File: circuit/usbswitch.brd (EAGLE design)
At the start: 100 x 80 mm, 11 parts, among them IC1 TINY25, Q2 BSA223SP

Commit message: cleanup
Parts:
- removed Q2: BSA223SP, irf:SO8
- added Q1: BSL207SP, irf:SOT23
- added R5, R6: 68, resistor:R1206
- moved D2 1.12 mm to (25.3, 34.6)
- moved R4 0.80 mm to (25.0, 31.9)
- moved D1 0.61 mm to (20.9, 33.9)
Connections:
- new net N$3: R5.2, X2.2
- new net N$8: R6.2, X2.3
- net N$1: now also Q1.1; no longer Q2.4
- net N$2: now also Q1.3; no longer Q2.5, Q2.6, Q2.7, Q2.8
- net VCC: now also Q1.2, R5.1, R6.1; no longer Q2.1, Q2.2, Q2.3
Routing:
- net VCC: track 27.9 -> 43.9 mm
- net N$2: track 18.5 -> 12.7 mm
- net N$3: track 0.00 -> 4.14 mm
- net N$8: track 0.00 -> 3.57 mm
- net N$1: track 2.72 -> 3.87 mm
- net N$4: track 22.9 -> 21.8 mm
- net N$5: track 9.86 -> 9.30 mm
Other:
- board size 100 x 80 mm -> 21.5 x 43.5 mm

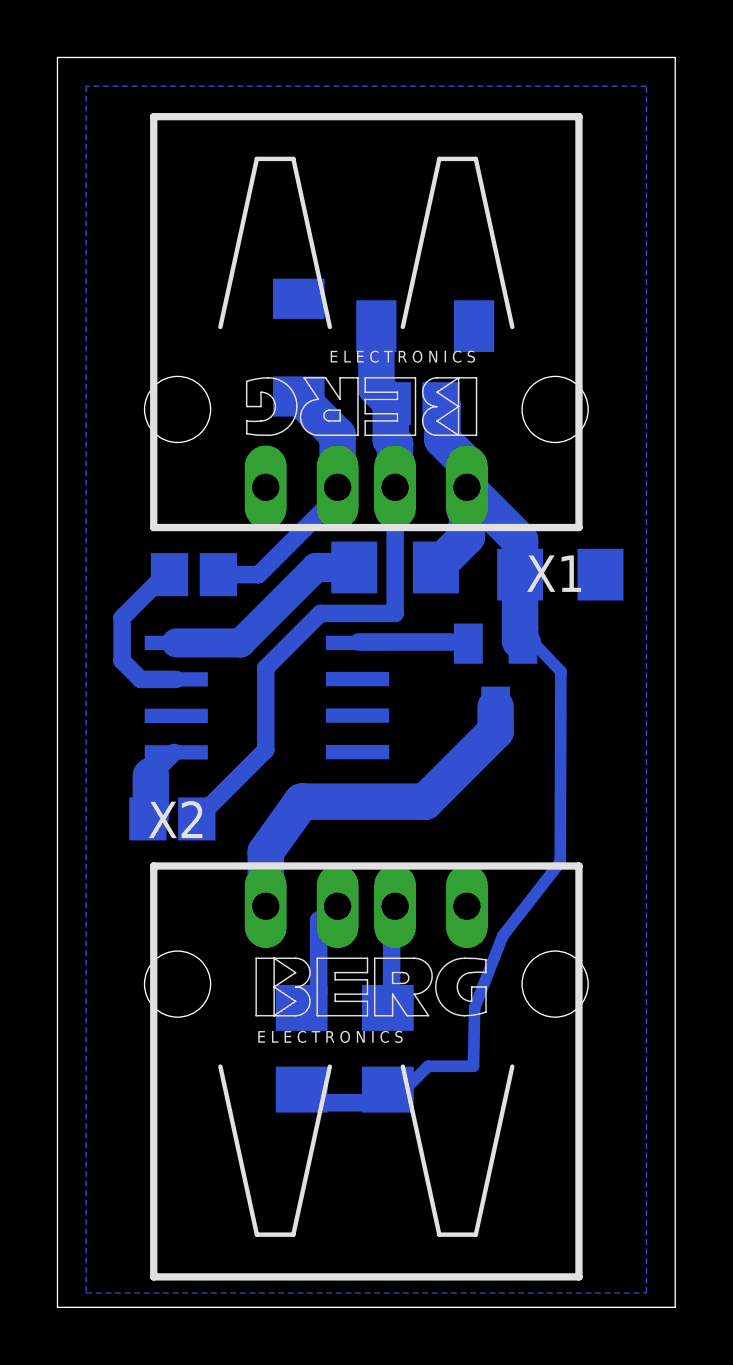
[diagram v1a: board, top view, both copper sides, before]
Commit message: Lessons learned from first smd prototype
* turned USB connector to PC around
* made all resistors 1206 types
* still need to fix transistor stuff...
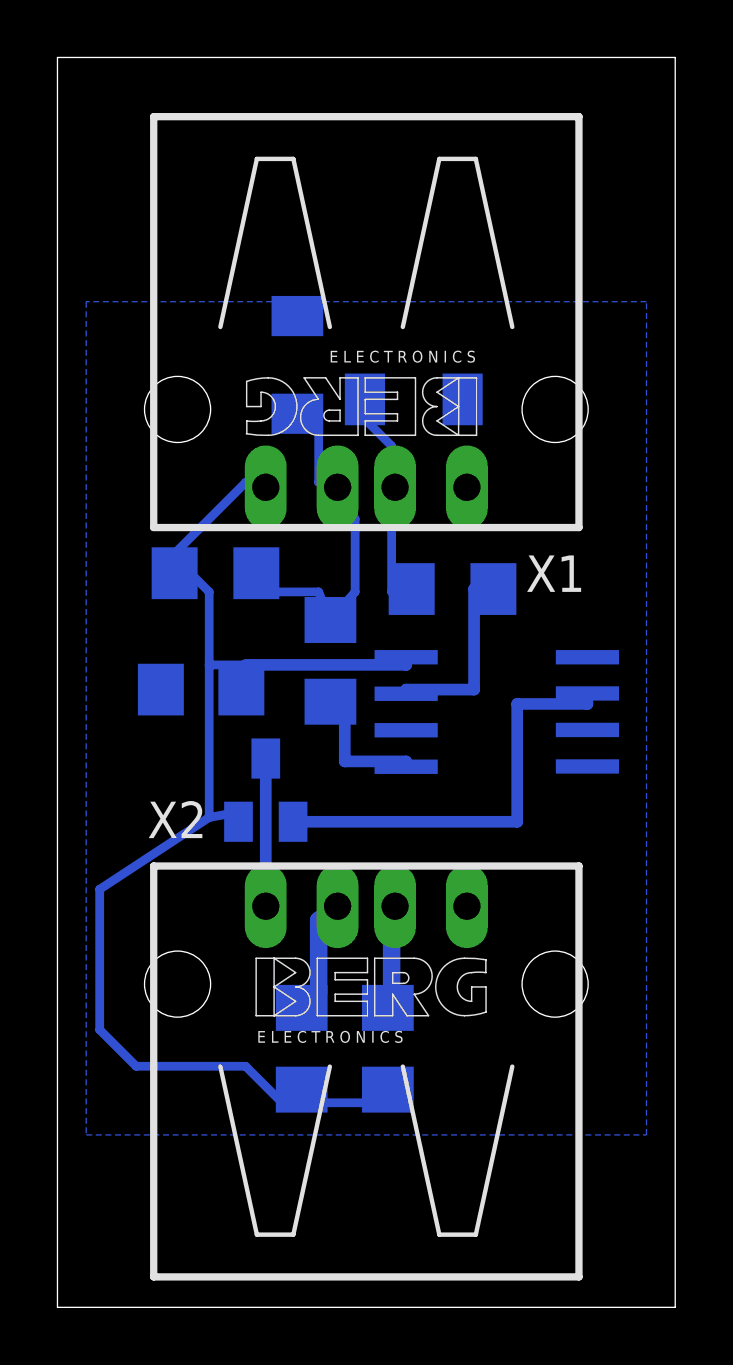
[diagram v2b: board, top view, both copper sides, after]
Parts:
- removed R1: 68, resistor:R1206
- R2, R3, R4: device resistor:R0805 -> rcl:R1206
- R6: device resistor:R1206 -> rcl:R1206
- moved C1 13.1 mm to (17.5, 22.0), turned to 0 degrees
- moved R4 9.15 mm to (18.0, 26.1), turned to 0 degrees
- moved R3 9.01 mm to (26.2, 25.5), turned to 180 degrees
- moved Q1 8.94 mm to (19.8, 18.5), turned to 0 degrees
- moved IC1 8.02 mm to (27.8, 21.2)
- moved R2 7.78 mm to (22.0, 23.0), turned to 270 degrees
- moved D2 4.65 mm to (20.9, 33.3), turned to 90 degrees
- moved D1 4.39 mm to (24.9, 32.1), turned to 180 degrees
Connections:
- net GND: now also X1.1; no longer X1.4
- net N$1: now also IC1.2; no longer IC1.1
- net N$4: now also X1.3; no longer X1.2
- net N$5: now also X1.2; no longer X1.3
- net VCC: now also X1.4; no longer R1.1, R1.2, X1.1
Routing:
- net N$1: track 3.87 -> 14.7 mm
- net N$4: track 21.8 -> 13.4 mm
- net N$2: track 12.7 -> 5.14 mm
- net N$6: track 2.77 -> 5.61 mm
- net VCC: track 43.9 -> 46.5 mm
- net N$5: track 9.30 -> 8.11 mm
- net N$7: track 5.92 -> 6.68 mm
